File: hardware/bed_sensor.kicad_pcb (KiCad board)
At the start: 2 copper layers, 41 x 36 mm, 32 parts, among them J1 Conn_01x02, J2 Conn_01x06, J3 ISP, J4 Conn_01x02, J5 DM3AT-SF-PEJM5, Q1 2N2219, SW1 SW_SPST, U1 MIC5205-3.3, U2 MPU-9250, U3 ATMEGA328-AU, U5 CFAH0802D-YYH-JP, Y1 Crystal_GND2

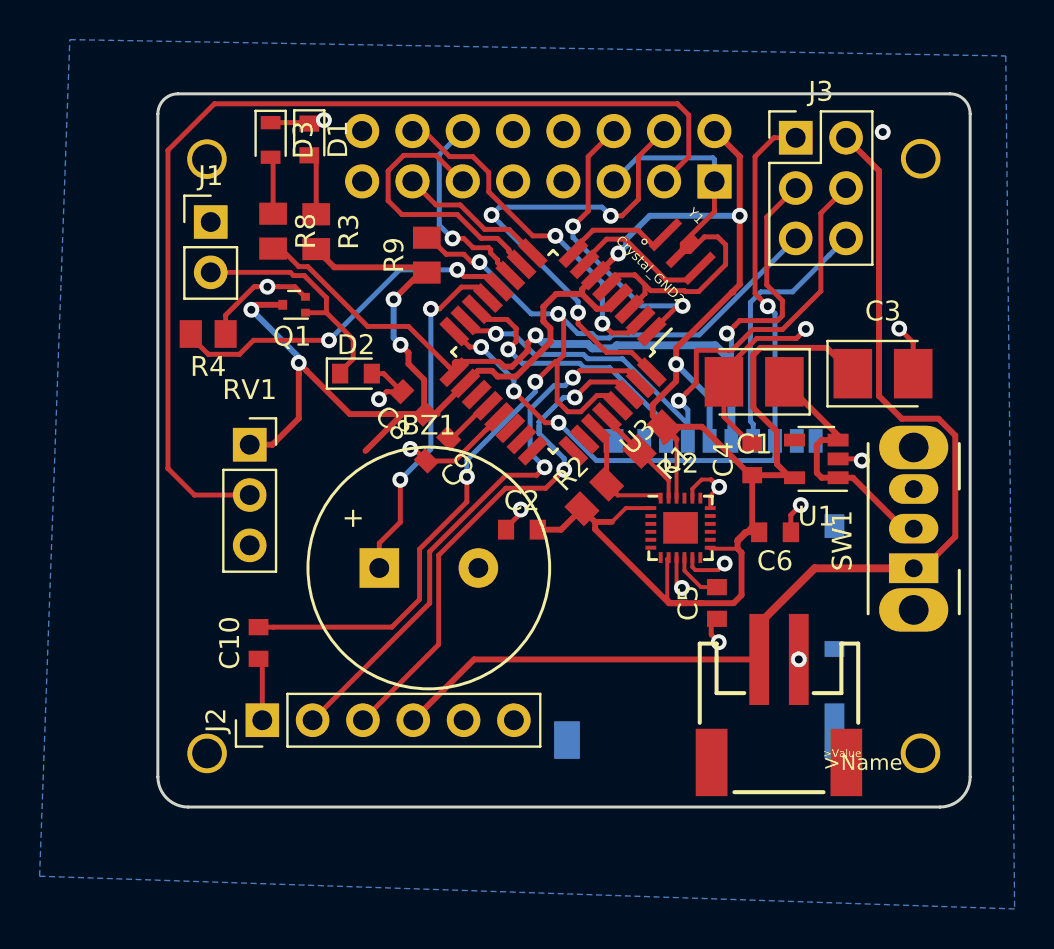
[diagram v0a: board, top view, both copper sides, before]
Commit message: modified design slightly and fixed problems with layout
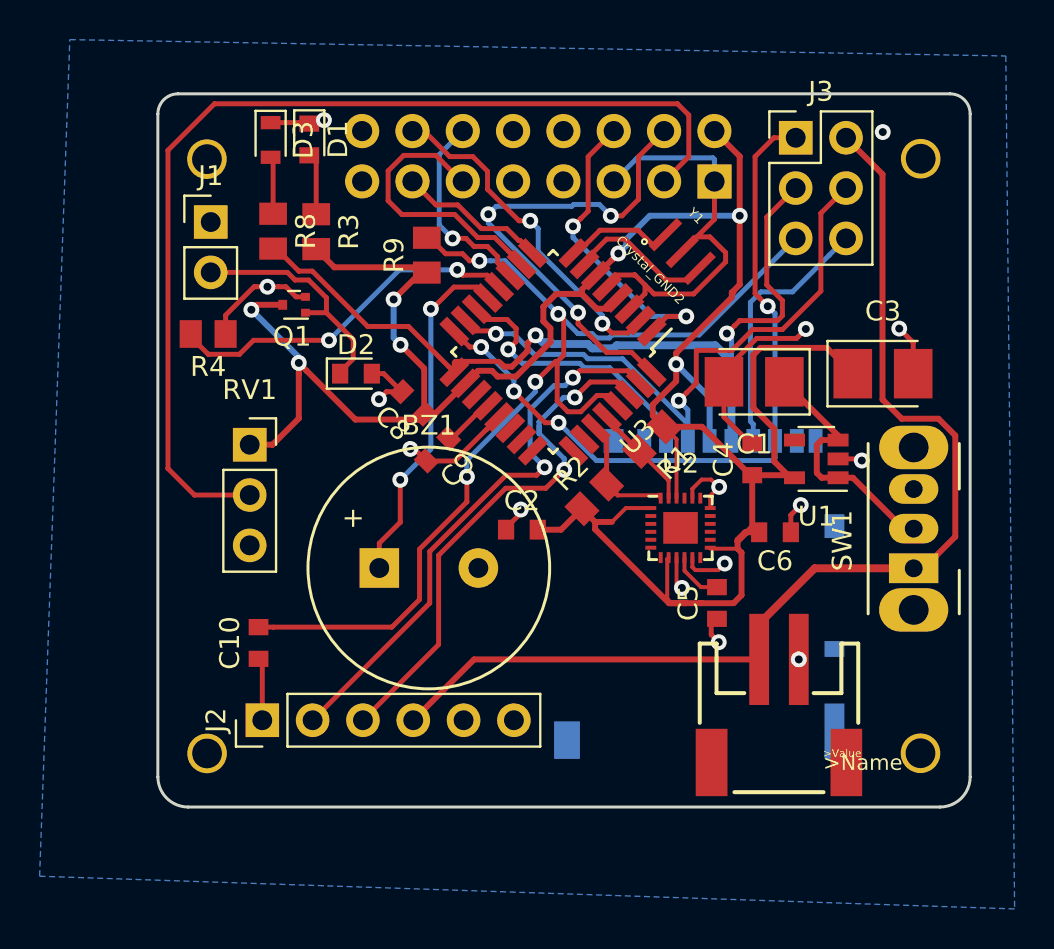
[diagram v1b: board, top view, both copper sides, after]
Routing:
- net +3V3: track 139.1 -> 134.2 mm
- net GND: track 74.7 -> 74.0 mm
